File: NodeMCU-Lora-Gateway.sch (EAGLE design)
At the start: 28 parts, among them IC1 ATSHA204A, J2 GROVE-I2C, J3 Lipo Battery, J4 GROVE-I2C, J5 CON_HEADER_1X08-PTH, P1 PADSMALL, P2 PADNORMAL, Q1 BSS84, U1 RFM9x

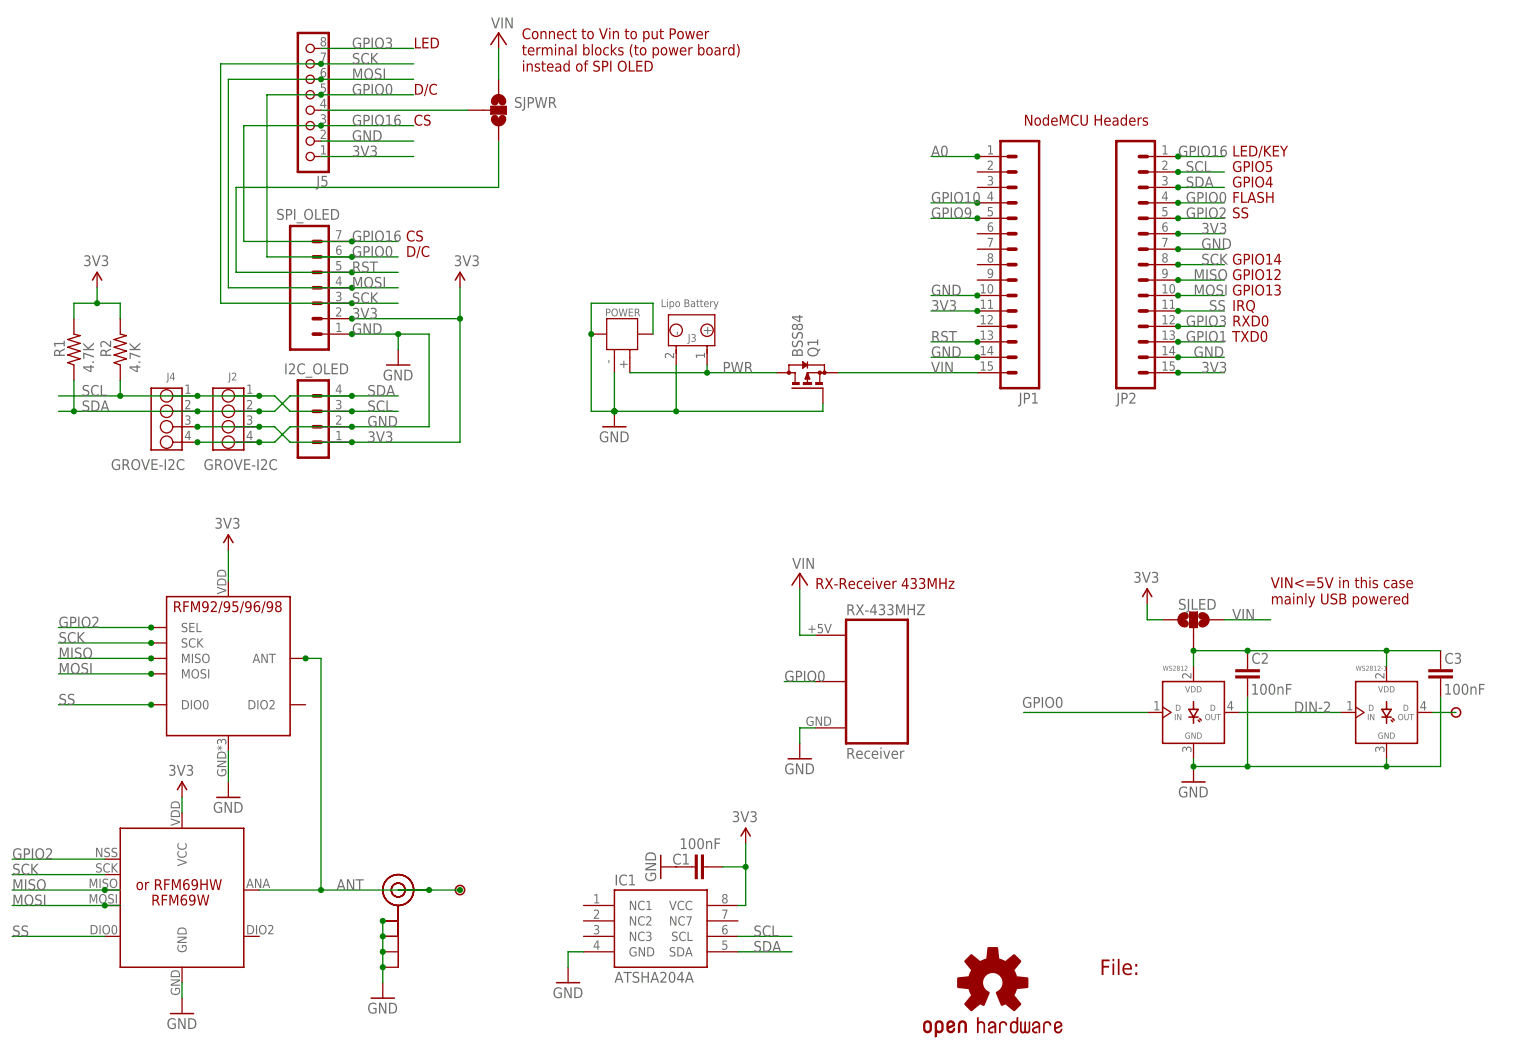
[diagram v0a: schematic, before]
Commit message: Bump to V1.3 version
* SMA/UFL Antenna connector has been size reduced
* Antenna trace and RF Module surrounded with via for better RF
isolation
* Increased "Isolate" ground planes to avoid shorts between connectors
and ground (may happen sometimes after soldering)
* I2C OLED connector is now "lock" version, you can just plug to test it
will fit without connector
* No more LED solder pad to choose VIN/3V3, added 1N4148 diode from 5V
for the 1st LED to decrease VCC to 4.4V, always works
* LORA version, added Microchip 64 bits Unique ID footprint 24AA02E64
* LORA version, done a diode logic OR for DIO0/DIO1/DIO2 for current
LIMC implementation
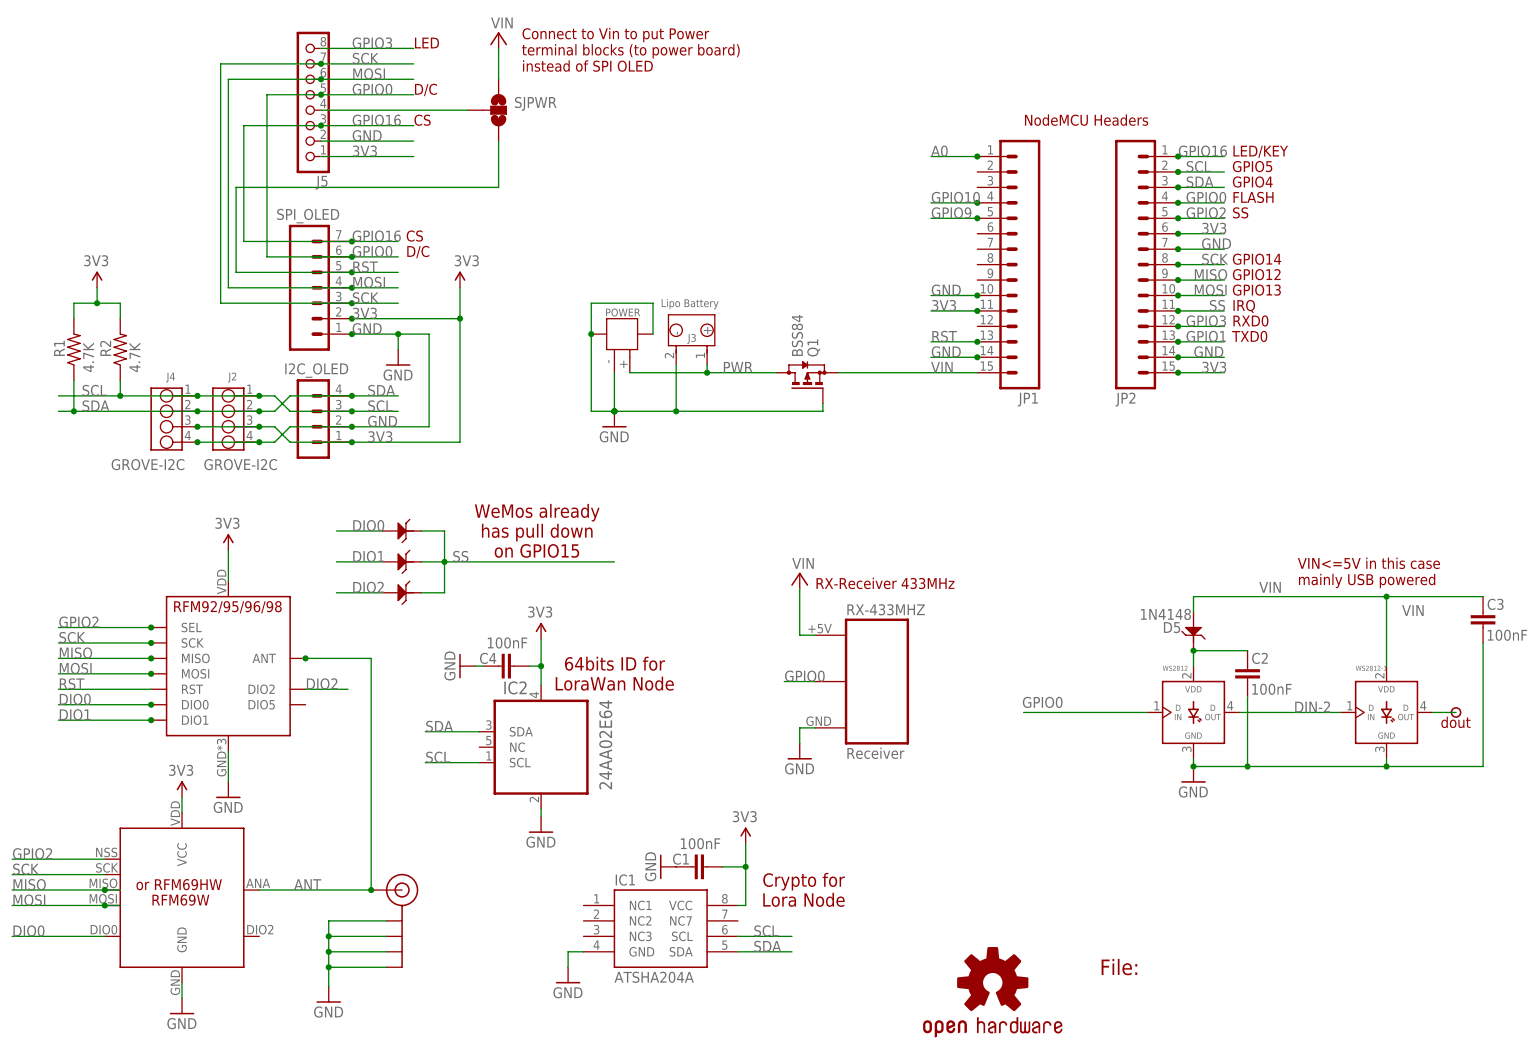
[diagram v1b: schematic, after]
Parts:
- removed P1: PADSMALL, SteveMarple:PADSMALL
- removed SJLED: JUMPER-PAD-3-2OF3_NC_BY_TRACE_LARGE, SparkFun-Passives:JUMPER-PAD-3-2OF3_NC_BY_TRACE_LARGE
- removed U-FL: U.FL, microbuilder:U.FL
- added C4: 100nF, _c2h:CAP0805-CAP
- added D0, D1, D2, D5: 1N4148, Seeed-Discrete:D-ESD-2P-CESD5V0D1
- added IC2: 24AA02E64, Microchip-24AA02E64T:24AA02E64T-I/OT
- I2C_OLED: value CON_HEADER_1X04'SMALL'' -> CON_HEADER_1X04'LOCK'; device _c2h:CON_HEADER_1X04'SMALL'' -> _c2h:CON_HEADER_1X04'LOCK'
- J$1: value SMA_EDGE -> ANTENNATINY; device SparkFun-Connectors:SMA_EDGE -> _c2h:ANTENNATINY
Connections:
- new net DIO0: D0.1, U$3.DIO0, U1.DIO0
- new net DIO1: D1.1, U1.DIO1
- new net DIO2: D2.1, U1.DIO2
- net 3V3: now also C4.2, IC2.VCC; no longer SJLED.3
- net ANT: no longer P1.1, U-FL.SIGNAL
- net GND: now also C4.1, IC2.VSS; no longer U-FL.GND@0, U-FL.GND@1
- net RST: now also U1.RST
- net SCL: now also IC2.SCL
- net SDA: now also IC2.SDA
- net SS: now also D0.2, D1.2, D2.2; no longer U$3.DIO0, U1.DIO0
- net VIN: now also C3.2, D5.1, WS2812-1.VDD; no longer SJLED.1
- net VLED: now also D5.2; no longer C3.2, SJLED.2, WS2812-1.VDD
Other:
- note added: "64bits ID for LoraWan Node"
- note added: "Crypto for Lora Node"
- note added: "WeMos already has pull down on GPIO15"
- note added: "dout"
- moved on the sheet: C3
